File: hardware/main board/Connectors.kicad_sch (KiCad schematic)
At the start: 26 parts, among them J1 USB4145-03-0070-C, J10 M80-5100622, J11 M80-5101422, J14 Conn_01x05, J16 TagConnect, J2 M80-5100442, J3 M80-5100442, J4 M300-MV10345M1, J5 M300-MV10345M1, J6 M80-5100442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

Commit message: done power plane layout
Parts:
- removed J2, J3: M80-5100442, Samacsys:M80-51004YY, symbol Samacsys2:M80-5100442
- removed J7: M80-5100622, Samacsys:M80-51006YY, symbol Samacsys2:M80-5100622
- removed J8: M80-5102022, Samacsys:M80-51020YY, symbol Samacsys2:M80-5102022
- added J2: M80-5103422, Samacsys:M80-51034YY, symbol Samacsys2:M80-5103422
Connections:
- net AIR_M_DETECTION: now also J2.11
- net AIR_PRE_DETECTION: now also J2.12
- net AIR_P_DETECTION: now also J2.28
- net AMS_FAULT_COCKPIT: now also J2.21
- net AMS_SAFETY_1: now also J2.4
- net AMS_SAFETY_2: now also J2.5
- net BOOT0: now also J2.9
- net CANFD1+: now also J2.27
- net CANFD1-: now also J2.26
- net CANFD2+: now also J2.25
- net CANFD2-: now also J2.24
- net CHARGER_DETECTION: now also J2.6
- net D+: now also J2.7
- net D-: now also J2.8
- net EXT_RESET: now also J2.22
- net GND: now also J2.16, J2.17, J2.20, J2.23, J2.29, J2.3, J2.30, J2.34
- net IMD_SENSENSOR: now also J2.13
- net MISO_C: now also J2.33
- net MOSI_C: now also J2.32
- net SAFETY_TSMS_IN: now also J2.1, J2.18
- net SCK_C: now also J2.31
- net VBUS: now also J2.10
- net VDD: now also J2.19, J2.2
- net ~{EXT_CS_I}_C: now also J2.14
- net ~{EXT_CS_V}_C: now also J2.15
- no-connect marks 6 -> 5
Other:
- note removed: "Air Detect"
- note removed: "Ext Measure"
- note removed: "IMD Sens"
- moved on the sheet: J11, J14, J16, J9

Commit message: repairing demaged branch~
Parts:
- added R72: 10M, Resistor_SMD:R_2512_6332Metric, symbol Device:R_Small
- H4: footprint MountingHole:MountingHole_3.2mm_M3_Pad_Via -> MountingHole:MountingHole_3.2mm_M3; symbol Mechanical:MountingHole_Pad -> Mechanical:MountingHole
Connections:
- net AIR_M_DETECTION: now also J2.13; no longer J2.11
- net BOOT0: now also J2.29; no longer J2.9
- net CANFD1+: now also J2.7; no longer J2.27
- net CANFD1-: now also J2.24; no longer J2.26
- net CANFD2+: now also J2.8; no longer J2.25
- net CANFD2-: now also J2.25; no longer J2.24
- net CHARGER_DETECTION: now also J2.10; no longer J2.6
- net D+: no longer J2.7
- net D-: no longer J2.8
- net EXT_RESET: now also J2.11; no longer J2.22
- net GND: now also J2.22, J2.26, J2.27, J2.6, J2.9, R72.1; no longer J2.16, J2.17, J2.29, J2.30, J2.34
- net IMD_SENSENSOR: now also J2.30; no longer J2.13
- net LTC_CHASSIS: now also R72.2; no longer H4.1
- net VBUS: no longer J2.10
- new net EX_D+: J2.17
- new net EX_D-: J2.16
- new net EX_VBUS: J2.34
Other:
- moved on the sheet: C28, C29, R37, R53, T1

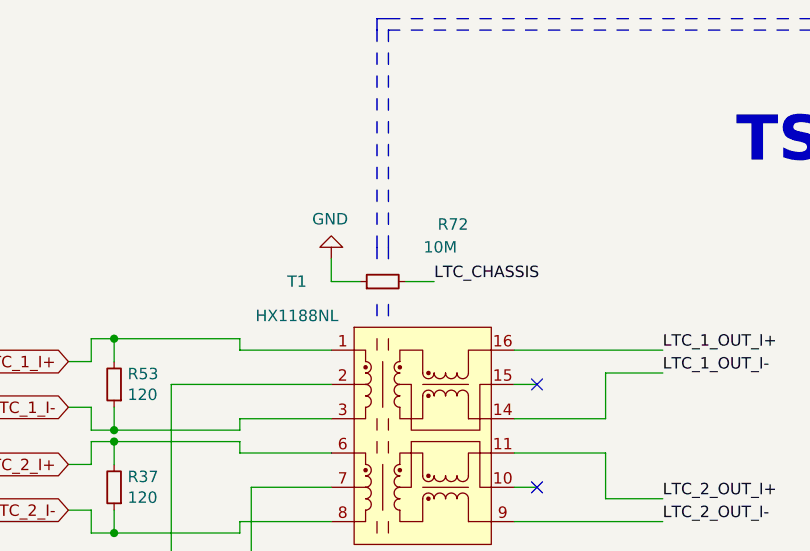
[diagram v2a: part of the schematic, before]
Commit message: slight changes, changed shield's coupling resitor to a couplingcapacitor
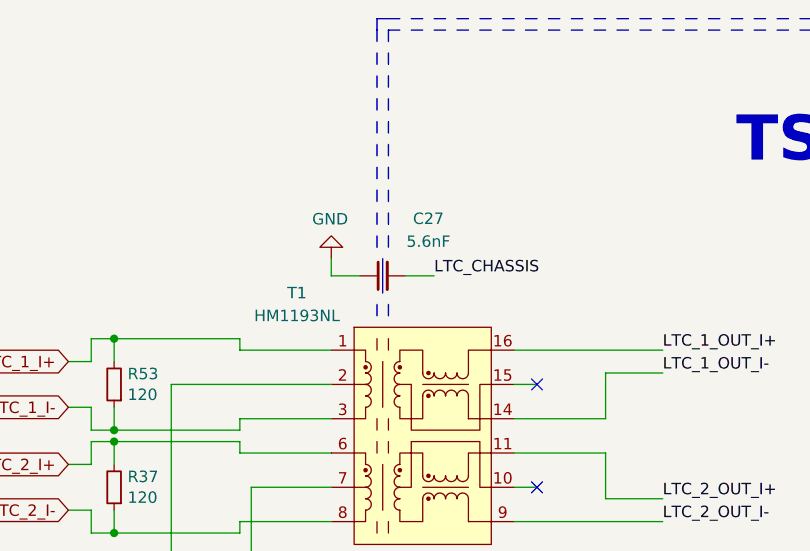
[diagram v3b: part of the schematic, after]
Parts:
- removed R72: 10M, Resistor_SMD:R_2512_6332Metric, symbol Device:R_Small
- added C27: 5.6nF, Samacsys:C2824, symbol c2824c562jggacauto:C2824C562JGGACAUTO
- T1: value HX1188NL -> HM1193NL; Manufacturer_Name (none) -> Harwin; Manufacturer_Part_Number (none) -> HM1193NL; Mouser Part Number (none) -> 673-HM1193NL; Mouser Price/Stock (none) -> https://www.mouser.pl/ProductDetail/Pulse-Electronics/HM119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
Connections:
- net GND: now also C27.1
- net LTC_CHASSIS: now also C27.2
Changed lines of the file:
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@@
+    (stroke (width 0.15) (type default) (color 132 0 0 1))
+  )
+  (polyline (pts (xy 182.245 41.91) (xy 182.245 45.72))
     (stroke (width 0.15) (type default) (color 132 0 0 1))
   )
@@
     (stroke (width 0.15) (type default) (color 132 0 0 1))
   )
-  (wire (pts (xy 176.53 44.45) (xy 179.705 44.45))
+  (wire (pts (xy 176.53 43.815) (xy 179.705 43.815))
     (stroke (width 0) (type default))
   )
@@
     (stroke (width 0.15) (type default) (color 132 0 0 1))
   )
-  (wire (pts (xy 184.785 44.45) (xy 187.96 44.45))
+  (wire (pts (xy 184.785 43.815) (xy 187.96 43.815))
     (stroke (width 0) (type default))
   )
@@
     (stroke (width 0) (type default))
   )
-  (polyline (pts (xy 182.88 40.64) (xy 182.88 41.91))
-    (stroke (width 0.15) (type default) (color 132 0 0 1))
-  )
   (polyline (pts (xy 215.9 15.24) (xy 217.17 15.24))
     (stroke (width 0.15) (type default) (color 132 0 0 1))
@@
     (stroke (width 0.15) (type default) (color 132 0 0 1))
   )
-  (polyline (pts (xy 181.61 40.64) (xy 181.61 41.91))
-    (stroke (width 0.15) (type default) (color 132 0 0 1))
-  )
   (wire (pts (xy 55.88 166.37) (xy 58.42 166.37))
     (stroke (width 0) (type default))
@@
     (stroke (width 0.15) (type default) (color 132 0 0 1))
   )
-  (wire (pts (xy 176.53 41.91) (xy 176.53 44.45))
+  (wire (pts (xy 176.53 41.91) (xy 176.53 43.815))
     (stroke (width 0) (type default))
   )
@@
     (effects (font (size 1.27 1.27)) (justify right bottom))
   )
-  (label "LTC_CHASSIS" (at 187.96 44.45 0) (fields_autoplaced)
+  (label "LTC_CHASSIS" (at 187.96 43.815 0) (fields_autoplaced)
     (effects (font (size 1.27 1.27)) (justify left bottom))
   )
@@
         (path "/b456cffc-d9d7-4c91-91f2-36ec9a65dd1b/568caa85-d8c4-4885-aabf-c5422dff8b33"
           (reference "#PWR053") (unit 1)
+        )
+      )
+    )
+  )
+  (symbol (lib_id "c2824c562jggacauto:C2824C562JGGACAUTO") (at 182.245 43.815 0) (unit 1)
+    (in_bom yes) (on_board yes) (dnp no)
+    (property "Reference" "C27" (at 187.325 37.465 0)
+      (effects (font (size 1.27 1.27)))
+    )
+    (property "Value" "5.6nF" (at 187.325 40.005 0)
+      (effects (font (size 1.27 1.27)))
+    )
+    (property "Footprint" "Samacsys:C2824" (at 191.135 42.545 0)
+      (effects (font (size 1.27 1.27)) (justify left) hide)
+    )
+    (property "Datasheet" "https://content.kemet.com/datasheets/KEM_C1080_C0G_HV_AUTO_SMD.pdf" (at 191.135 45.085 0)
+      (effects (font (size 1.27 1.27)) (justify left) hide)
+    )
+    (property "Description" "SMD Auto C0G HV, Ceramic, 5600 pF, 5%, 2000 VDC, 2400 VDC, 125C, -55C, C0G, SMD, MLCC, Ultra-Stable, Low Loss, High Voltage, Automotive Grade, 0.1 % , 100 GOhms, 540 mg, 2824, 7.1mm, 6.1mm, 2.5mm, 1.27mm, 300, 78  Weeks, 120" (at 191.135 47.625 0)
+      (effects (font (size 1.27 1.27)) (justify left) hide)
+    )
+    (property "Height" "" (at 191.135 50.165 0)
+      (effects (font (size 1.27 1.27)) (justify left) hide)
+    )
+    (property "Mouser Part Number" "80-C2824C562JGGAUTO" (at 191.135 52.705 0)
+      (effects (font (size 1.27 1.27)) (justify left) hide)
+    )
+    (property "Mouser Price/Stock" "https://www.mouser.co.uk/ProductDetail/KEMET/C2824C562JGGACAUTO?qs=5aG0NVq1C4xKMWO6DzsxHA%3D%3D" (at 191.135 55.245 0)
+      (effects (font (size 1.27 1.27)) (justify left) hide)
+    )
+    (property "Manufacturer_Name" "KEMET" (at 191.135 57.785 0)
+      (effects (font (size 1.27 1.27)) (justify left) hide)
+    )
+    (property "Manufacturer_Part_Number" "C2824C562JGGACAUTO" (at 191.135 60.325 0)
+      (effects (font (size 1.27 1.27)) (justify left) hide)
+    )
+    (pin "1")
+    (pin "2")
+    (instances
+      (project "PUTM_EV_BMS_HV_Master_2021"
+        (path "/b456cffc-d9d7-4c91-91f2-36ec9a65dd1b/568caa85-d8c4-4885-aabf-c5422dff8b33"
+          (reference "C27") (unit 1)
         )
       )
@@
         (path "/b456cffc-d9d7-4c91-91f2-36ec9a65dd1b/568caa85-d8c4-4885-aabf-c5422dff8b33"
           (reference "#PWR088") (unit 1)
-        )
-      )
-    )
-  )
-  (symbol (lib_id "Device:R_Small") (at 182.245 44.45 90) (unit 1)
-    (in_bom yes) (on_board yes) (dnp no)
-    (property "Reference" "R72" (at 191.77 38.1 90)
-      (effects (font (size 1.27 1.27)) (justify left))
-    )
-    (property "Value" "10M" (at 190.5 40.64 90)
-      (effects (font (size 1.27 1.27)) (justify left))
-    )
-    (property "Footprint" "Resistor_SMD:R_2512_6332Metric" (at 182.245 44.45 0)
-      (effects (font (size 1.27 1.27)) hide)
-    )
-    (property "Datasheet" "~" (at 182.245 44.45 0)
-      (effects (font (size 1.27 1.27)) hide)
-    )
-    (pin "1")
-    (pin "2")
-    (instances
-      (project "PUTM_EV_BMS_HV_Master_2021"
-        (path "/b456cffc-d9d7-4c91-91f2-36ec9a65dd1b"
-          (reference "R72") (unit 1)
-        )
-        (path "/b456cffc-d9d7-4c91-91f2-36ec9a65dd1b/568caa85-d8c4-4885-aabf-c5422dff8b33"
-          (reference "R25") (unit 1)
         )
       )
@@
   (symbol (lib_id "PUTM_EV_BMS_library:HX1188NL") (at 189.23 62.23 0) (unit 1)
     (in_bom yes) (on_board yes) (dnp no)
-    (property "Reference" "T1" (at 172.72 44.45 0)
+    (property "Reference" "T1" (at 172.72 45.72 0)
       (effects (font (size 1.27 1.27)))
     )
-    (property "Value" "HX1188NL" (at 172.72 48.26 0)
+    (property "Value" "HM1193NL" (at 172.72 48.26 0)
       (effects (font (size 1.27 1.27)))
     )
@@
       (effects (font (size 1.27 1.27)) hide)
     )
-    (pin "1")
+    (property "Description" "Audio Transformers / Signal Transformers MDL SIN 100D 1:1 SMT AEC-Q200" (at 189.23 62.23 0)
+      (effects (font (size 1.27 1.27)) (justify left) hide)
+    )
+    (property "Height" "" (at 189.23 62.23 0)
+      (effects (font (size 1.27 1.27)) (justify left) hide)
+    )
+    (property "Manufacturer_Name" "Harwin" (at 189.23 62.23 0)
+      (effects (font (size 1.27 1.27)) (justify left) hide)
+    )
+    (property "Manufacturer_Part_Number" "HM1193NL" (at 189.23 62.23 0)
+      (effects (font (size 1.27 1.27)) (justify left) hide)
+    )
+    (property "Mouser Part Number" "673-HM1193NL" (at 189.23 62.23 0)
+      (effects (font (size 1.27 1.27)) (justify left) hide)
+    )
+    (property "Mouser Price/Stock" "https://www.mouser.pl/ProductDetail/Pulse-Electronics/HM1193NL?qs=%252B6g0mu59x7JcSK4q%2FgPx%252Bg%3D%3D" (at 189.23 62.23 0)
+      (effects (font (size 1.27 1.27)) (justify left) hide)
+    )
+    (property "Arrow Part Number" "" (at 189.23 62.23 0)
+      (effects (font (size 1.27 1.27)) (justify left) hide)
+    )
+    (property "Arrow Price/Stock" "" (at 189.23 62.23 0)
+      (effects (font (size 1.27 1.27)) (justify left) hide)
+    )
+    (pin "1")

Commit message: production version
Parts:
- C27: Manufacturer_Name KEMET -> (none)
- C28, C29: value 27nF -> 22nF; Manufacturer_Name (none) -> --; Manufacturer_Part_Number (none) -> --
- D21: Manufacturer_Part_Number (none) -> TSZU52C13 RGG; Mouser Part Number (none) -> 821-TSZU52C13RGG; Mouser Price/Stock (none) -> https://www.mouser.pl/ProductDetail/Taiwan-Semiconductor/TS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
- D8: Manufacturer_Part_Number (none) -> SP0505BAHTG; Mouser Part Number (none) -> 576-SP0505BAHTG; Mouser Price/Stock (none) -> https://www.mouser.pl/ProductDetail/Littelfuse/SP0505BAHTG?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
- F1: Manufacturer_Part_Number (none) -> 0ZCH0050FF2G; Mouser Part Number (none) -> 530-0ZCH0050FF2G; Mouser Price/Stock (none) -> https://www.mouser.pl/ProductDetail/Bel-Fuse/0ZCH0050FF2G?q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
- H4, J14, J16, R18, R19: Manufacturer_Name (none) -> --; Manufacturer_Part_Number (none) -> --
- R37, R53: value 120 -> 120R; Manufacturer_Name (none) -> --; Manufacturer_Part_Number (none) -> --
- RN2: value 33 -> 33R; Manufacturer_Part_Number (none) -> 742C163470JP; Mouser Part Number (none) -> 774-742C163470JP; Mouser Price/Stock (none) -> https://www.mouser.pl/ProductDetail/CTS-Electronic-Componen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
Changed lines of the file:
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@@
       (effects (font (size 1.27 1.27)) (justify left) hide)
     )
-    (property "Manufacturer_Name" "KEMET" (at 191.135 57.785 0)
+    (property "Manufacturer_Name" "" (at 191.135 57.785 0)
       (effects (font (size 1.27 1.27)) (justify left) hide)
     )
@@
       (effects (font (size 1.27 1.27)) hide)
     )
+    (property "Manufacturer_Part_Number" "0ZCH0050FF2G" (at 157.48 176.53 0)
+      (effects (font (size 1.27 1.27)) hide)
+    )
+    (property "Mouser Part Number" "530-0ZCH0050FF2G" (at 157.48 176.53 0)
+      (effects (font (size 1.27 1.27)) hide)
+    )
+    (property "Mouser Price/Stock" "https://www.mouser.pl/ProductDetail/Bel-Fuse/0ZCH0050FF2G?qs=SRYZG9HaIQ2VrAxOxbTdxQ%3D%3D" (at 157.48 176.53 0)
+      (effects (font (size 1.27 1.27)) hide)
+    )
     (pin "1")
     (pin "2")
@@
     )
     (property "Datasheet" "~" (at 260.35 93.98 0)
+      (effects (font (size 1.27 1.27)) hide)
+    )
+    (property "Manufacturer_Name" "--" (at 260.35 93.98 0)
+      (effects (font (size 1.27 1.27)) hide)
+    )
+    (property "Manufacturer_Part_Number" "--" (at 260.35 93.98 0)
       (effects (font (size 1.27 1.27)) hide)
     )
@@
       (effects (font (size 1.27 1.27)) (justify right))
     )
-    (property "Value" "120" (at 153.8986 68.453 0)
+    (property "Value" "120R" (at 153.8986 68.453 0)
       (effects (font (size 1.27 1.27)) (justify right))
     )
@@
     )
     (property "Datasheet" "~" (at 152.4 67.31 0)
+      (effects (font (size 1.27 1.27)) hide)
+    )
+    (property "Manufacturer_Name" "--" (at 152.4 67.31 0)
+      (effects (font (size 1.27 1.27)) hide)
+    )
+    (property "Manufacturer_Part_Number" "--" (at 152.4 67.31 0)
       (effects (font (size 1.27 1.27)) hide)
     )
@@
       (effects (font (size 1.27 1.27)) hide)
     )
+    (property "Manufacturer_Part_Number" "TSZU52C13 RGG" (at 137.16 181.61 0)
+      (effects (font (size 1.27 1.27)) hide)
+    )
+    (property "Mouser Part Number" "821-TSZU52C13RGG" (at 137.16 181.61 0)
+      (effects (font (size 1.27 1.27)) hide)
+    )
+    (property "Mouser Price/Stock" "https://www.mouser.pl/ProductDetail/Taiwan-Semiconductor/TSZU52C13-RGG?qs=QEzMiVqgwc2bkL9Eiq5VbQ%3D%3D" (at 137.16 181.61 0)
+      (effects (font (size 1.27 1.27)) hide)
+    )
     (pin "1")
     (pin "2")
@@
     )
     (property "Datasheet" "~" (at 118.11 97.79 0)
+      (effects (font (size 1.27 1.27)) hide)
+    )
+    (property "Manufacturer_Name" "--" (at 118.11 97.79 0)
+      (effects (font (size 1.27 1.27)) hide)
+    )
+    (property "Manufacturer_Part_Number" "--" (at 118.11 97.79 0)
       (effects (font (size 1.27 1.27)) hide)
     )
@@
       (effects (font (size 1.27 1.27)) hide)
     )
+    (property "Manufacturer_Name" "--" (at 256.54 148.59 0)
+      (effects (font (size 1.27 1.27)) hide)
+    )
+    (property "Manufacturer_Part_Number" "--" (at 256.54 148.59 0)
+      (effects (font (size 1.27 1.27)) hide)
+    )
     (pin "1")
     (pin "2")
@@
     )
     (property "Datasheet" "http://www.littelfuse.com/~/media/files/littelfuse/technical%20resources/documents/data%20sheets/sp05xxba.pdf" (at 74.295 117.475 0)
+      (effects (font (size 1.27 1.27)) hide)
+    )
+    (property "Manufacturer_Part_Number" "SP0505BAHTG" (at 77.47 120.65 0)
+      (effects (font (size 1.27 1.27)) hide)
+    )
+    (property "Mouser Part Number" "576-SP0505BAHTG" (at 77.47 120.65 0)
+      (effects (font (size 1.27 1.27)) hide)
+    )
+    (property "Mouser Price/Stock" "https://www.mouser.pl/ProductDetail/Littelfuse/SP0505BAHTG?qs=%2FvxM1TNbkdRUGqLTdRy61Q%3D%3D" (at 77.47 120.65 0)
       (effects (font (size 1.27 1.27)) hide)
     )
@@
       (effects (font (size 1.27 1.27)) hide)
     )
+    (property "Manufacturer_Part_Number" "TSZU52C13 RGG" (at 133.35 181.61 0)
+      (effects (font (size 1.27 1.27)) hide)
+    )
+    (property "Mouser Part Number" "821-TSZU52C13RGG" (at 133.35 181.61 0)
+      (effects (font (size 1.27 1.27)) hide)
+    )
+    (property "Mouser Price/Stock" "https://www.mouser.pl/ProductDetail/Taiwan-Semiconductor/TSZU52C13-RGG?qs=QEzMiVqgwc2bkL9Eiq5VbQ%3D%3D" (at 133.35 181.61 0)
+      (effects (font (size 1.27 1.27)) hide)
+    )
     (pin "1")
     (pin "2")
@@
       (effects (font (size 1.27 1.27)) hide)
     )
+    (property "Manufacturer_Name" "--" (at 124.46 127 0)
+      (effects (font (size 1.27 1.27)) hide)
+    )
+    (property "Manufacturer_Part_Number" "--" (at 124.46 127 0)
+      (effects (font (size 1.27 1.27)) hide)
+    )
     (pin "1")
     (pin "2")
@@
       (effects (font (size 1.27 1.27)) (justify left))
     )
-    (property "Value" "27nF" (at 161.0868 79.883 0)
+    (property "Value" "22nF" (at 161.0868 79.883 0)
       (effects (font (size 1.27 1.27)) (justify left))
     )
@@
     )
     (property "Datasheet" "~" (at 158.75 78.74 0)
+      (effects (font (size 1.27 1.27)) hide)
+    )
+    (property "Manufacturer_Name" "--" (at 158.75 78.74 0)
+      (effects (font (size 1.27 1.27)) hide)
+    )
+    (property "Manufacturer_Part_Number" "--" (at 158.75 78.74 0)
       (effects (font (size 1.27 1.27)) hide)
     )
@@
       (effects (font (size 1.27 1.27)))
     )
-    (property "Value" "33" (at 35.56 100.33 90)
+    (property "Value" "33R" (at 35.56 100.33 90)
       (effects (font (size 1.27 1.27)))
     )
@@
     )
     (property "Datasheet" "~" (at 35.56 113.03 0)
+      (effects (font (size 1.27 1.27)) hide)
+    )
+    (property "Manufacturer_Part_Number" "742C163470JP" (at 35.56 113.03 0)
+      (effects (font (size 1.27 1.27)) hide)
+    )
+    (property "Mouser Part Number" "774-742C163470JP" (at 35.56 113.03 0)
+      (effects (font (size 1.27 1.27)) hide)
+    )
+    (property "Mouser Price/Stock" "https://www.mouser.pl/ProductDetail/CTS-Electronic-Components/742C163470JP?qs=hbgUSdfWRJXHiW0nNtpaOg%3D%3D" (at 35.56 113.03 0)
       (effects (font (size 1.27 1.27)) hide)
     )
@@
       (effects (font (size 1.27 1.27)) hide)
     )
+    (property "Manufacturer_Name" "--" (at 254 148.59 0)
+      (effects (font (size 1.27 1.27)) hide)
+    )
+    (property "Manufacturer_Part_Number" "--" (at 254 148.59 0)
+      (effects (font (size 1.27 1.27)) hide)
+    )
     (pin "1")
     (pin "2")
@@
       (effects (font (size 1.27 1.27)) (justify left))
     )
-    (property "Value" "27nF" (at 169.9768 79.883 0)
+    (property "Value" "22nF" (at 169.9768 79.883 0)
       (effects (font (size 1.27 1.27)) (justify left))
     )
@@
     )
     (property "Datasheet" "~" (at 167.64 78.74 0)
+      (effects (font (size 1.27 1.27)) hide)
+    )
+    (property "Manufacturer_Name" "--" (at 167.64 78.74 0)
+      (effects (font (size 1.27 1.27)) hide)
+    )
+    (property "Manufacturer_Part_Number" "--" (at 167.64 78.74 0)
       (effects (font (size 1.27 1.27)) hide)
     )
@@
       (effects (font (size 1.27 1.27)) (justify right))
     )
-    (property "Value" "120" (at 153.8986 57.023 0)
+    (property "Value" "120R" (at 153.8986 57.023 0)
       (effects (font (size 1.27 1.27)) (justify right))
     )
@@
       (effects (font (size 1.27 1.27)) hide)
     )
+    (property "Manufacturer_Name" "--" (at 152.4 55.88 0)
+      (effects (font (size 1.27 1.27)) hide)
+    )
+    (property "Manufacturer_Part_Number" "--" (at 152.4 55.88 0)
+      (effects (font (size 1.27 1.27)) hide)
+    )
